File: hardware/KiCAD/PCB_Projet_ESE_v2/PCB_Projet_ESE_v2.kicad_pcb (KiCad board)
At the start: 6 copper layers, 52 x 52 mm, 111 parts, among them J1 Conn_01x06, J10 Conn_ST_STDC14, J2 Conn_01x06, J4 Conn_01x03, J5 Conn_01x04, J6 Conn_01x04, J9 Conn_01x02, SW1 SW_SPST, SW2 472121010111, SW3 SW_SPST, SW5 472121010111, U1 ZXBM5210-SP, U2 ZXBM5210-SP, U3 NCS210, U4 NCS210, U5 STM32G474RETx, U6 ADXL343, Y1 Crystal_GND24_Small

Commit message: first version 52*52mm
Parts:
- removed H2, H3, H4: MountingHole_Pad, MountingHole:MountingHole_3.2mm_M3_Pad_Via
- removed SW2: 472121010111, mylib:472123010111
- added C49: D8L6.5_865090349007, Capacitor_SMD_Wurth:CP_Wurth_WCAP-ASLU-D8L6.5, B.Cu at (156.4, 78.2)
- added SW4: SW_SPDT, mylib:472123010111, F.Cu at (198.2, 74.0)
- BUxxSD1, C10, C13, C14, C15, C16, C17, C2, C34, C35, C36, C37, C38, C39, C40, C41, C42, C44, C46, C48, C5, C7, C8, C9, D1, F1, J6, L2, MP1, R1, R15, R16, R17, R18, R19, R20, R3, R4, U2, U3, U7, U8, U9: moved to B.Cu
- H1: footprint MountingHole:MountingHole_3.2mm_M3_Pad_Via -> MountingHole:MountingHole_2.2mm_M2_Pad_Via
- SW5: value 472121010111 -> SW_SPDT
- moved Y1 102.5 mm to (190.2, 67.0)
- moved D1 98.3 mm to (186.4, 57.8), turned to 45 degrees
- moved R10 94.9 mm to (185.2, 67.2)
- moved R9 94.5 mm to (185.1, 66.1), turned to 180 degrees
- moved C9 94.3 mm to (192.9, 61.5), turned to -45 degrees
- moved R8 93.4 mm to (188.8, 83.3), turned to 90 degrees
- moved R7 92.1 mm to (187.8, 83.3), turned to 90 degrees
- moved R14 87.9 mm to (187.0, 94.8), turned to -90 degrees
- moved C2 87.6 mm to (189.9, 80.2), turned to 90 degrees
- moved R4 87.6 mm to (179.4, 79.7)
- moved C3 87.4 mm to (189.0, 91.3), turned to 135 degrees
- moved R3 87.0 mm to (178.9, 78.1), turned to -90 degrees
- moved SW1 86.9 mm to (162.7, 58.3), turned to 135 degrees
- moved R13 86.1 mm to (185.3, 94.8), turned to -90 degrees
- moved C21 85.7 mm to (193.5, 70.8)
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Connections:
- SW5 pad 1: Mode_1 -> +7.4V
- SW5 pad 2: +3.3V -> Net-(J9-Pin_2)
- SW5 pad 3: Mode_2 -> unconnected-(SW5-C-Pad3)
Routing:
- added copper zone on B.Cu, net (none)
- added copper zone on F.Cu, net (none)
- added copper zone on In1.Cu, net (none)
- added copper zone on In2.Cu, net (none)
- added copper zone on In4.Cu, net (none)
- added copper zone on In3.Cu, net +3.3V
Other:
- outline, holes or cut-outs redrawn

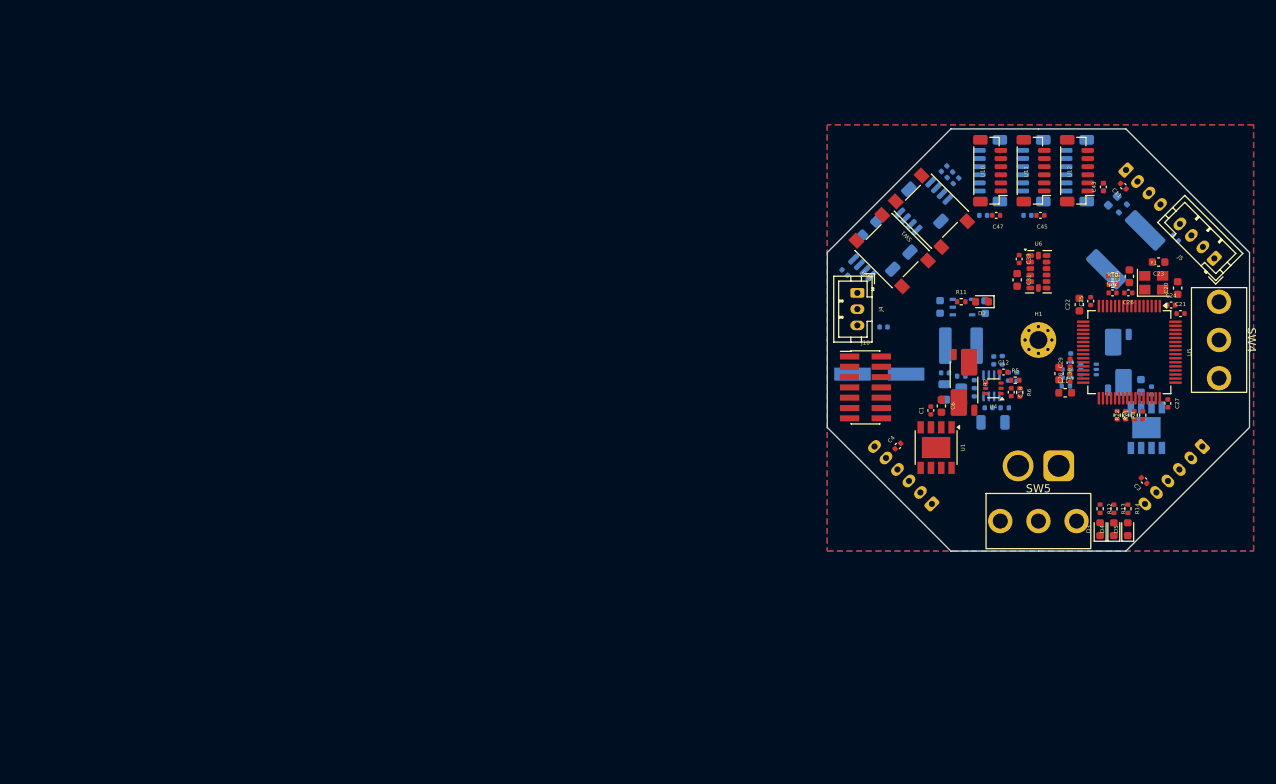
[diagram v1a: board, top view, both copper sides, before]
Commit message: new version 47x47mm
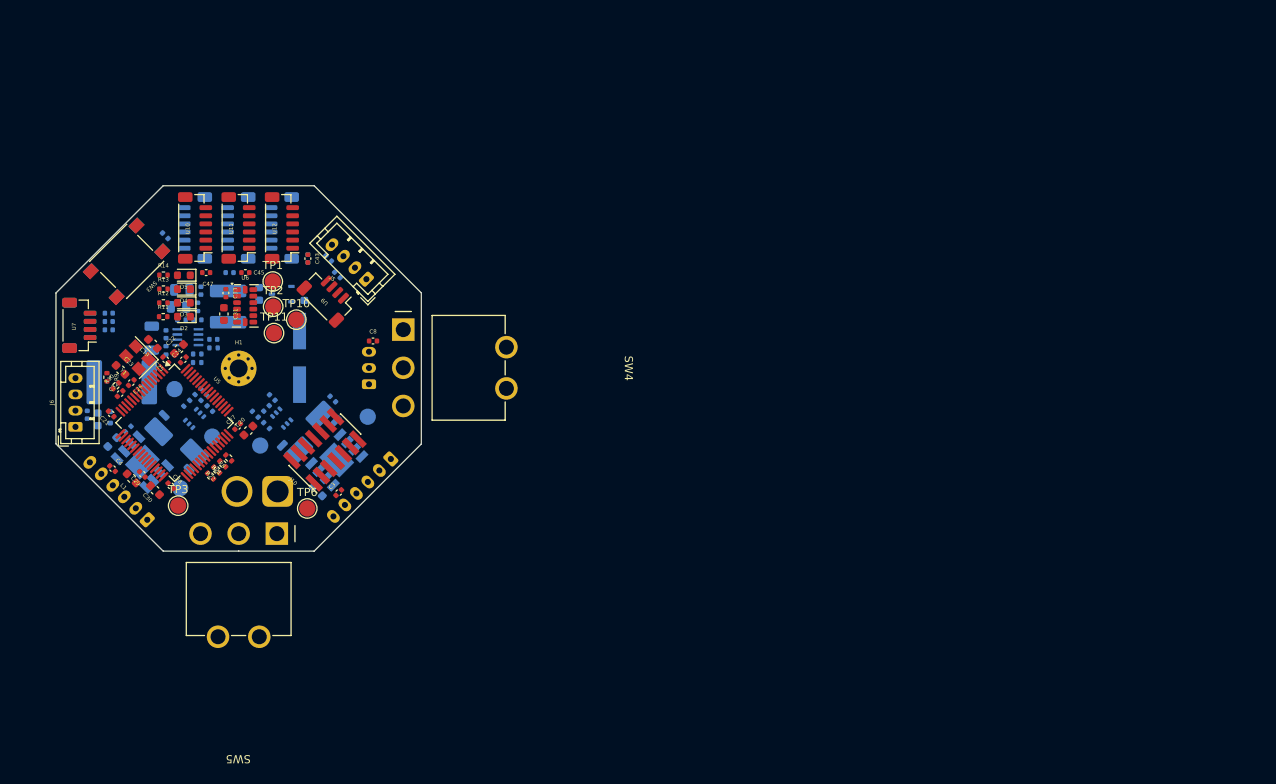
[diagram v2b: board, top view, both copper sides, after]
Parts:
- added TP1: TestPoint, TestPoint:TestPoint_Pad_D2.0mm, F.Cu at (81.7, 66.8)
- added TP10: TestPoint, TestPoint:TestPoint_Pad_D2.0mm, F.Cu at (84.6, 71.5)
- added TP11: TestPoint, TestPoint:TestPoint_Pad_D2.0mm, F.Cu at (81.8, 73.2)
- added TP2: TestPoint, TestPoint:TestPoint_Pad_D2.0mm, F.Cu at (81.8, 69.9)
- added TP3: TestPoint, TestPoint:TestPoint_Pad_D2.0mm, F.Cu at (70.0, 94.4)
- added TP4: TestPoint, TestPoint:TestPoint_Pad_D2.0mm, B.Cu at (80.2, 87.0)
- added TP5: TestPoint, TestPoint:TestPoint_Pad_D2.0mm, B.Cu at (74.2, 85.9)
- added TP6: TestPoint, TestPoint:TestPoint_Pad_D2.0mm, F.Cu at (86.0, 94.8)
- added TP7: TestPoint, TestPoint:TestPoint_Pad_D2.0mm, B.Cu at (93.4, 83.5)
- added TP8: TestPoint, TestPoint:TestPoint_Pad_D2.0mm, B.Cu at (70.3, 92.2)
- added TP9: TestPoint, TestPoint:TestPoint_Pad_D2.0mm, B.Cu at (69.6, 80.0)
- C1, C11, C12, C18, C6, J4, R2, R5, R6, SW1, U1, U4: moved to B.Cu
- C8, J6, U7, U9: moved to F.Cu
- SW4, SW5: footprint mylib:472123010111 -> mylib:SW_Wurth_WS-TOTV_472123020421
- moved J6 133.2 mm to (57.4, 84.7), turned to 90 degrees
- moved C21 132.3 mm to (61.8, 83.1), turned to 135 degrees
- moved C11 130.7 mm to (58.9, 83.2), turned to -90 degrees
- moved C23 128.5 mm to (63.0, 77.7), turned to -45 degrees
- moved C14 127.9 mm to (60.1, 83.8), turned to -90 degrees
- moved D1 127.4 mm to (61.7, 83.5), turned to 90 degrees
- moved Y1 125.5 mm to (65.0, 76.2), turned to 135 degrees
- moved F1 124.7 mm to (63.1, 79.2), turned to 0 degrees
- moved R9 124.5 mm to (61.3, 78.6), turned to -90 degrees
- moved R10 123.4 mm to (62.4, 79.6), turned to 45 degrees
- moved C26 123.3 mm to (64.3, 79.2), turned to -135 degrees
- moved C32 122.9 mm to (62.9, 80.6), turned to 45 degrees
- moved R14 122.2 mm to (68.2, 66.0), turned to 0 degrees
- moved C24 121.8 mm to (70.7, 76.4), turned to 45 degrees
- moved C19 120.6 mm to (66.9, 74.5), turned to 135 degrees
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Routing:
- removed copper zone on B.Cu, net (none)
- removed copper zone on F.Cu, net (none)
- removed copper zone on In1.Cu, net (none)
- removed copper zone on In2.Cu, net (none)
- removed copper zone on In4.Cu, net (none)
- removed copper zone on In3.Cu, net +3.3V
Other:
- board size 52 x 52 mm -> 45 x 45 mm

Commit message: routage en cours
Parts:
- removed D1: D_TVS_Small, Diode_SMD:D_SOD-523
- added C50: 100n, Capacitor_SMD:C_0402_1005Metric, F.Cu at (91.8, 79.0)
- added C51: 100n, Capacitor_SMD:C_0402_1005Metric, B.Cu at (82.8, 70.7)
- added C52: 100n, Capacitor_SMD:C_0402_1005Metric, F.Cu at (87.7, 67.3)
- added C53: 100n, Capacitor_SMD:C_0402_1005Metric, F.Cu at (91.9, 74.3)
- added C54: 1u, Capacitor_SMD:C_0402_1005Metric, B.Cu at (83.3, 65.9)
- added C55: 1u, Capacitor_SMD:C_0402_1005Metric, B.Cu at (89.9, 66.5)
- added C56: 10u, Capacitor_SMD:C_0603_1608Metric, B.Cu at (92.3, 67.8)
- added C57: 10u, Capacitor_SMD:C_0603_1608Metric, B.Cu at (95.1, 71.3)
- added C58: 100n, Capacitor_SMD:C_0402_1005Metric, F.Cu at (84.2, 67.9)
- added C59: 100n, Capacitor_SMD:C_0402_1005Metric, F.Cu at (82.3, 65.7)
- added C60: 100n, Capacitor_SMD:C_0402_1005Metric, F.Cu at (80.4, 65.7)
- added C61: 100n, Capacitor_SMD:C_0402_1005Metric, F.Cu at (78.5, 66.7)
- added C62: 100n, Capacitor_SMD:C_0402_1005Metric, F.Cu at (95.2, 72.8)
- added C63: 100n, Capacitor_SMD:C_0402_1005Metric, F.Cu at (84.2, 69.8)
- added C64: 100n, Capacitor_SMD:C_0402_1005Metric, F.Cu at (86.2, 67.3)
- added C65: 100n, Capacitor_SMD:C_0402_1005Metric, F.Cu at (94.1, 68.2)
- added C66: 100n, Capacitor_SMD:C_0402_1005Metric, F.Cu at (95.5, 69.0)
- added C67: 100n, Capacitor_SMD:C_0402_1005Metric, F.Cu at (96.2, 69.7)
- added C68: 100n, Capacitor_SMD:C_0402_1005Metric, F.Cu at (83.8, 71.3)
- added C69: 100n, Capacitor_SMD:C_0402_1005Metric, F.Cu at (59.5, 86.7)
- added C70: 100n, Capacitor_SMD:C_0402_1005Metric, F.Cu at (68.0, 96.4)
- added C71: 100n, Capacitor_SMD:C_0402_1005Metric, F.Cu at (87.9, 97.1)
- added C72: 100n, Capacitor_SMD:C_0402_1005Metric, F.Cu at (96.5, 86.8)
- added D10: Yellow LED, LED_SMD:LED_0603_1608Metric, F.Cu at (83.7, 76.7)
- added D11: Yellow LED, LED_SMD:LED_0603_1608Metric, F.Cu at (83.6, 78.3)
- added D12: Orange LED, LED_SMD:LED_0603_1608Metric, F.Cu at (86.8, 73.5)
- added D13: Orange LED, LED_SMD:LED_0603_1608Metric, F.Cu at (86.8, 75.1)
- added D14: Amber LED, LED_SMD:LED_0603_1608Metric, F.Cu at (83.6, 79.9)
- added D15: Amber LED, LED_SMD:LED_0603_1608Metric, F.Cu at (83.7, 81.5)
- added D16: Red LED, LED_SMD:LED_0603_1608Metric, F.Cu at (86.8, 79.9)
- added D17: Red LED, LED_SMD:LED_0603_1608Metric, F.Cu at (86.8, 81.5)
- added D18: Super Red LED, LED_SMD:LED_0603_1608Metric, F.Cu at (86.8, 76.7)
- added D19: Super Red LED, LED_SMD:LED_0603_1608Metric, F.Cu at (86.8, 78.3)
- added D20: ~, Diode_SMD:D_SOD-523, B.Cu at (59.9, 83.6)
- added D6: Green LED, LED_SMD:LED_0603_1608Metric, F.Cu at (83.7, 73.5)
- added D7: YELLOW_LED, mylib:wurth_155060YS75300, F.Cu at (98.6, 68.7)
- added D8: YELLOW_LED, mylib:wurth_155060YS75300, F.Cu at (98.7, 84.9)
- added D9: Green LED, LED_SMD:LED_0603_1608Metric, F.Cu at (83.7, 75.1)
- added L3: 4u7, mylib:WE-TPC-744028004, B.Cu at (88.7, 68.0)
- added LM1: ~, Package_DFN_QFN:WQFN-16-1EP_3x3mm_P0.5mm_EP1.68x1.68mm, F.Cu at (81.6, 68.4)
- added LM2: ~, Package_DFN_QFN:WQFN-16-1EP_3x3mm_P0.5mm_EP1.68x1.68mm, F.Cu at (93.1, 71.1)
- added LM3: ~, Package_DFN_QFN:WQFN-16-1EP_3x3mm_P0.5mm_EP1.68x1.68mm, F.Cu at (86.9, 70.4)
- added R23: 300, Resistor_SMD:R_0402_1005Metric, F.Cu at (97.7, 69.4)
- added R24: 300, Resistor_SMD:R_0402_1005Metric, F.Cu at (97.7, 85.6)
- added R29: 48k7, Resistor_SMD:R_0402_1005Metric, F.Cu at (91.8, 81.1)
- added R30: 39k2, Resistor_SMD:R_0402_1005Metric, F.Cu at (91.8, 80.1)
- added R31: 3k3, Resistor_SMD:R_0402_1005Metric, F.Cu at (81.1, 74.9)
- added R32: 3k3, Resistor_SMD:R_0402_1005Metric, F.Cu at (81.1, 75.9)
- added R33: 1k6, Resistor_SMD:R_0402_1005Metric, F.Cu at (81.1, 77.0)
- added R34: 1k6, Resistor_SMD:R_0402_1005Metric, F.Cu at (81.1, 78.0)
- added R35: 2k, Resistor_SMD:R_0402_1005Metric, F.Cu at (81.1, 79.1)
- added R36: 2k, Resistor_SMD:R_0402_1005Metric, F.Cu at (81.1, 80.1)
- added R37: 1k, Resistor_SMD:R_0402_1005Metric, F.Cu at (89.3, 74.8)
- added R38: 1k, Resistor_SMD:R_0402_1005Metric, F.Cu at (89.3, 75.9)
- added R43: 1k3, Resistor_SMD:R_0402_1005Metric, F.Cu at (89.3, 76.9)
- added R44: 1k3, Resistor_SMD:R_0402_1005Metric, F.Cu at (89.3, 78.0)
- added R45: 2k4, Resistor_SMD:R_0402_1005Metric, F.Cu at (89.3, 79.0)
- added R46: 2k4, Resistor_SMD:R_0402_1005Metric, F.Cu at (89.3, 80.1)
- added R51: 5k23, Resistor_SMD:R_0201_0603Metric, B.Cu at (84.6, 65.8)
- added R52: 100k, Resistor_SMD:R_0201_0603Metric, B.Cu at (85.4, 65.8)
- added R53: 11k, Resistor_SMD:R_0201_0603Metric, B.Cu at (81.0, 65.5)
- added R54: 98k8, Resistor_SMD:R_0402_1005Metric, B.Cu at (79.2, 65.6)
- added R55: 20k, Resistor_SMD:R_0201_0603Metric, B.Cu at (79.2, 66.6)
- added R56: 79k6, Resistor_SMD:R_0402_1005Metric, B.Cu at (77.2, 66.0)
- added R57: 20k, Resistor_SMD:R_0201_0603Metric, B.Cu at (79.5, 70.6)
- added R58: 46k4, Resistor_SMD:R_0201_0603Metric, B.Cu at (81.0, 70.6)
- added R59: 20k, Resistor_SMD:R_0201_0603Metric, F.Cu at (95.4, 73.8)
- added R60: 30k, Resistor_SMD:R_0201_0603Metric, F.Cu at (93.9, 73.9)
- added R61: 47k, Resistor_SMD:R_0201_0603Metric, B.Cu at (96.6, 69.3)
- added R62: 47k, Resistor_SMD:R_0201_0603Metric, B.Cu at (98.1, 69.3)
- added R63: 30k, Resistor_SMD:R_0201_0603Metric, F.Cu at (97.3, 67.6)
- added R64: 20k, Resistor_SMD:R_0201_0603Metric, F.Cu at (96.5, 68.0)
- added R65: 46.4k, Resistor_SMD:R_0201_0603Metric, B.Cu at (95.2, 69.0)
- added R66: 20k, Resistor_SMD:R_0201_0603Metric, B.Cu at (94.6, 68.0)
- added R67: 79k6, Resistor_SMD:R_0402_1005Metric, B.Cu at (87.8, 66.1)
- added R68: 20k, Resistor_SMD:R_0201_0603Metric, B.Cu at (86.5, 66.1)
- added R69: 98k8, Resistor_SMD:R_0402_1005Metric, F.Cu at (84.7, 66.3)
- added R70: 11k, Resistor_SMD:R_0201_0603Metric, F.Cu at (85.2, 67.5)
- added R71: 100k, Resistor_SMD:R_0201_0603Metric, F.Cu at (84.0, 72.2)
- added R72: 5k23, Resistor_SMD:R_0201_0603Metric, F.Cu at (82.5, 72.2)
- added R73: 4k7, Resistor_SMD:R_0402_1005Metric, F.Cu at (72.8, 90.2)
- added R74: 4k7, Resistor_SMD:R_0402_1005Metric, F.Cu at (72.1, 91.0)
- added TP12: ~, Package_TO_SOT_SMD:SOT-23-5, B.Cu at (92.5, 70.7)
- added U16: MCP1802x-xx02xOT, Package_TO_SOT_SMD:SOT-23-5, B.Cu at (84.4, 68.2)
- C22, C30, C31, C41, C42: footprint Capacitor_SMD:C_0603_1608Metric -> Capacitor_SMD:C_0402_1005Metric
- C9: moved to F.Cu
- J5: footprint Connector_JST:JST_PH_B4B-PH-K_1x04_P2.00mm_Vertical -> Connector_THT_Wurth:J_Wurth_WR-WTB_62000411722; moved to B.Cu
- J6: footprint Connector_JST:JST_PH_B4B-PH-K_1x04_P2.00mm_Vertical -> Connector_THT_Wurth:J_Wurth_WR-WTB_62000411722
- R10: value 5k6 -> 16k
- R11: value 240 -> 39
- R12: value 2k9 -> 2k7
- R13: value 1k65 -> 1k6
- R14: value 800 -> 820
- R9: value 20k -> 56k
- TP3: moved to B.Cu
- moved R14 24.9 mm to (79.0, 88.4), turned to -90 degrees
- moved D5 24.8 mm to (81.0, 88.5)
- moved R13 23.9 mm to (83.2, 86.4), turned to -90 degrees
- moved D4 21.8 mm to (81.1, 86.9), turned to 0 degrees
- moved TP3 21.2 mm to (62.2, 74.7), turned to 180 degrees
- moved R12 21.2 mm to (83.2, 84.4), turned to -90 degrees
- moved D3 18.9 mm to (81.1, 85.2), turned to 0 degrees
- moved TP10 17.8 mm to (66.8, 69.8)
- moved TP2 14.1 mm to (68.0, 67.0)
- moved TP11 12.4 mm to (70.0, 69.8)
- moved TP1 10.7 mm to (71.0, 67.0)
- moved TP9 9.06 mm to (77.2, 85.0)
- moved D2 8.39 mm to (62.4, 71.5), turned to 0 degrees
- moved TP5 7.87 mm to (71.3, 78.6)
- moved C9 7.83 mm to (96.1, 66.2)
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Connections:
- SW4 pad G1: (no net) -> unconnected-(SW4-PadG1)
- SW4 pad G2: (no net) -> unconnected-(SW4-PadG2)
- SW5 pad G1: (no net) -> unconnected-(SW5-PadG1)
- SW5 pad G2: (no net) -> unconnected-(SW5-PadG2)
- U5 pad 19: TOF_1_XSHUT -> TOF_4_XSHUT
- U5 pad 21: TOF_2_XSHUT -> TOF_3_XSHUT
- U5 pad 23: TOF_4_XSHUT -> TOF_5_XSHUT
- U5 pad 33: TOF_5_XSHUT -> TOF_2_XSHUT
- U5 pad 38: TOF_SCL -> AMPLI_SCL
- U5 pad 39: TOF_SDA -> AMPLI_SDA
- U5 pad 40: AMPLI_SCL -> TOF_SCL
- U5 pad 41: AMPLI_SDA -> TOF_SDA
- U5 pad 44: TOF_3_XSHUT -> TOF_1_XSHUT
- U5 pad 59: TOF_3_GPIO -> TOF_5_GPIO
- U5 pad 60: TOF_4_GPIO -> TOF_3_GPIO
- U5 pad 61: unconnected-(U5-PB8-Pad61) -> GND
- U5 pad 62: TOF_5_GPIO -> TOF_4_GPIO
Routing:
- net GND: track 0.00 -> 147.2 mm, vias 0 -> 104
- net +3.3V: track 0.00 -> 76.3 mm, vias 0 -> 26
- net TOF_SCL: track 0.00 -> 59.5 mm, vias 0 -> 11
- net TOF_SDA: track 0.00 -> 57.7 mm, vias 0 -> 9
- net NRST: track 0.00 -> 54.5 mm, vias 0 -> 3
- net +5V: track 0.00 -> 50.5 mm, vias 0 -> 21
- net TOF_6_XSHUT: track 0.00 -> 47.5 mm, vias 0 -> 4
- net TOF_1_XSHUT: track 0.00 -> 47.3 mm, vias 0 -> 5
- net Mode_1: track 0.00 -> 45.7 mm, vias 0 -> 1
- net AMPLI_SDA: track 0.00 -> 44.5 mm, vias 0 -> 2
- net TOF_2_XSHUT: track 0.00 -> 43.2 mm, vias 0 -> 5
- net Mode_2: track 0.00 -> 39.9 mm, vias 0 -> 1
- net UART_LIDAR_TX_HD: track 0.00 -> 39.8 mm, vias 0 -> 2
- net PWM_LED: track 0.00 -> 37.2 mm, vias 0 -> 2
- net TOF_5_XSHUT: track 0.00 -> 37.2 mm, vias 0 -> 3
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- added copper zone on In3.Cu, net +3.3V
- added copper zone on In3.Cu, net +5V
- added copper zone on In3.Cu, net +7.4V
- added copper zone on B.Cu, net /5V_Rpi
- added copper zone on B.Cu, net GND
- added copper zone on F.Cu, net GND
- added copper zone on In1.Cu, net GND
- added copper zone on In2.Cu, net GND
- added copper zone on In4.Cu, net GND
- added copper zone on In3.Cu, net IN+
- added copper zone on In3.Cu, net Net-(J9-Pin_2)
